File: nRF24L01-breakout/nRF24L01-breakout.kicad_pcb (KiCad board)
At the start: 2 copper layers, 41 x 17.6 mm, 20 parts, among them J1 Conn_01x08_Female, U1 NRF24L01, U2 Antenna_PCB_2.4GHz_50Ohm, Y1 Crystal_GND24_Small

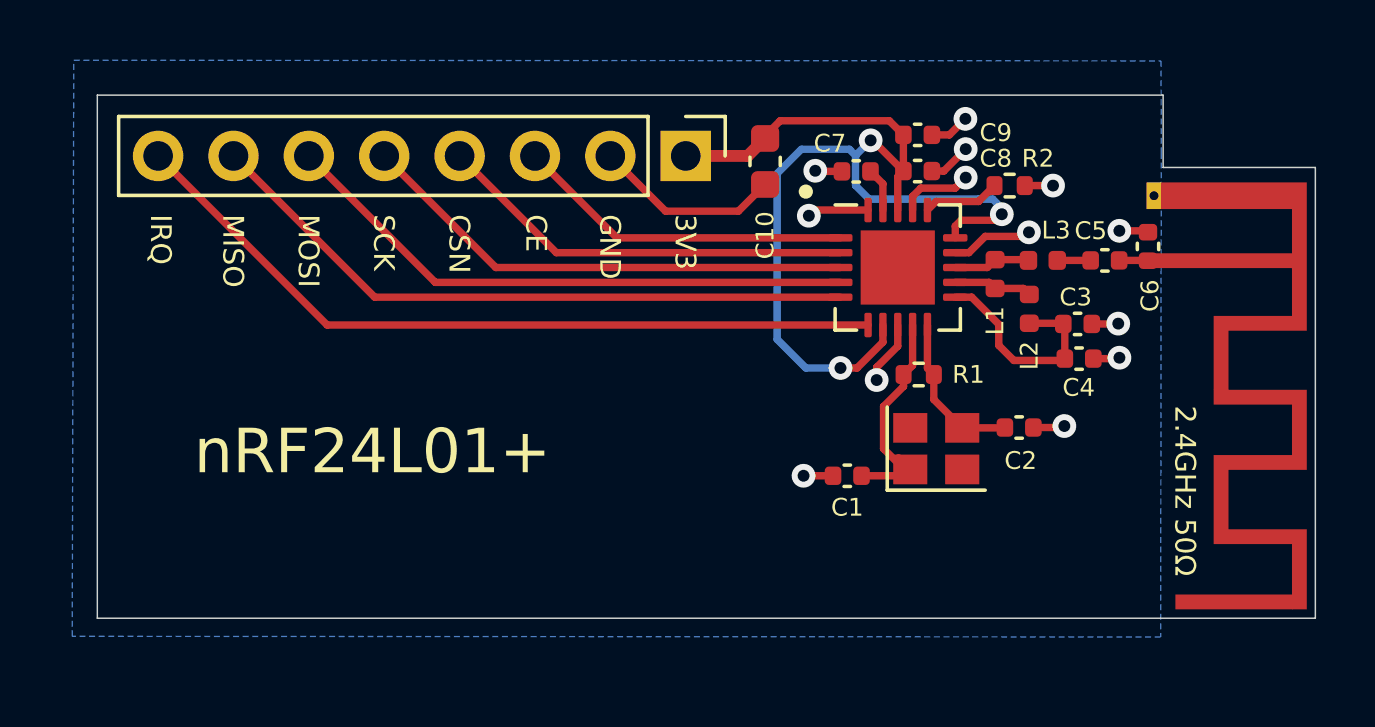
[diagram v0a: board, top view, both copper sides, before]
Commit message: Use Johanson 2450BM14A0002 matched balun
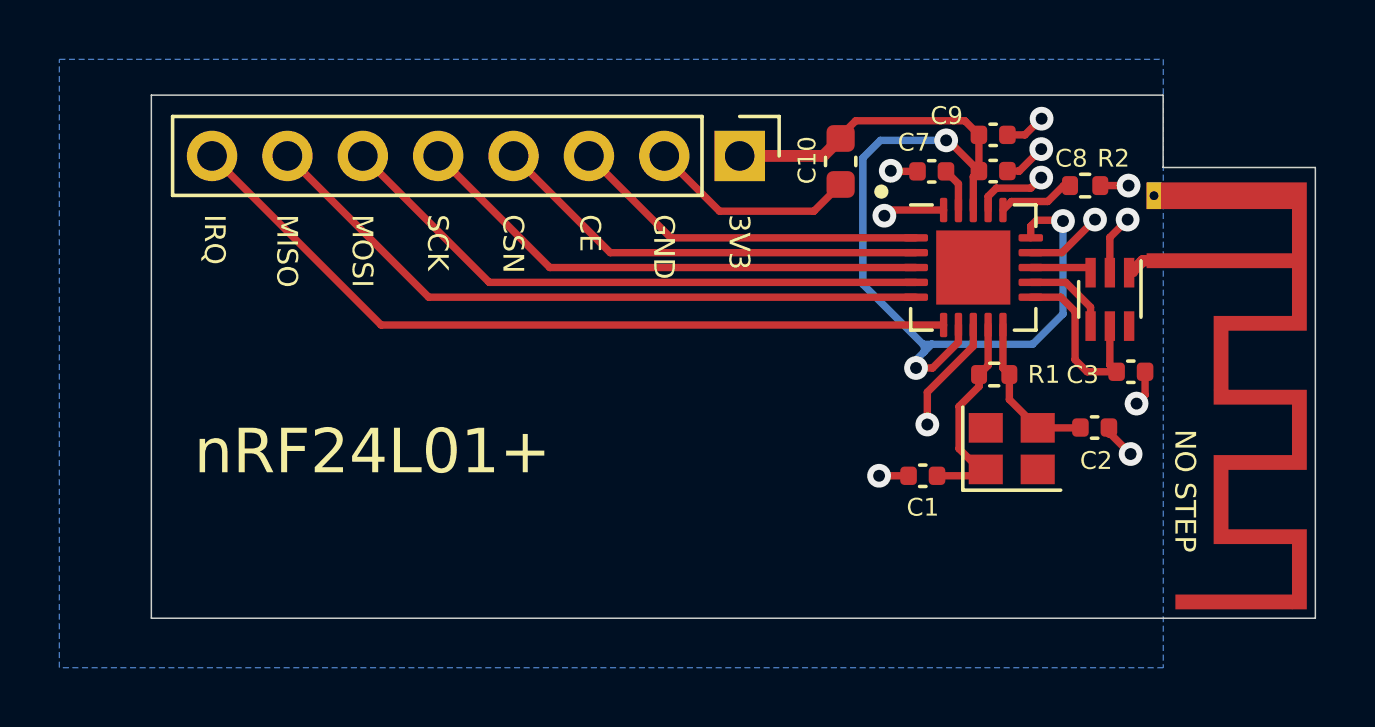
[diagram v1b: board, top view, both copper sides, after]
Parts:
- removed C4: 2.2nF, Capacitor_SMD:C_0402_1005Metric
- removed C5: 1.5pF, Capacitor_SMD:C_0402_1005Metric
- removed C6: 1pF, Capacitor_SMD:C_0402_1005Metric
- removed L1: 8.2nH, Inductor_SMD:L_0402_1005Metric
- removed L2: 2.7nH, Inductor_SMD:L_0402_1005Metric
- removed L3: 3.9nH, Inductor_SMD:L_0402_1005Metric
- added U3: Balun_2450BM14A0002, RF_Converter:Balun_Johanson_0896BM15A0001, F.Cu at (173.6, 90.8)
- moved C1 2.55 mm to (167.3, 96.7)
- moved C2 2.55 mm to (173.1, 95.1)
- moved R1 2.55 mm to (169.7, 93.3)
- moved R2 2.55 mm to (172.7, 86.9)
- moved U1 2.55 mm to (169.0, 89.7)
- moved Y1 2.55 mm to (170.3, 95.8)
- moved C10 2.54 mm to (164.5, 86.1)
- moved C7 2.54 mm to (167.6, 86.4)
- moved C8 2.54 mm to (169.6, 86.4)
- moved C9 2.54 mm to (169.6, 85.2)
- moved C3 2.41 mm to (174.3, 93.2)
- moved J1 1.82 mm to (161.1, 85.9)
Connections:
- net +3V3 renamed VDD
- U2 pad 1: Net-(C5-Pad2) -> Net-(U2-Pad1)
- U2 pad 2: GND -> Net-(U2-Pad1)
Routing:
- net Net-(U2-Pad1): track 0.00 -> 3.31 mm
- net GND: track 25.4 -> 28.6 mm, vias 13 -> 12
- net VDD: track 35.1 -> 36.6 mm
- net Net-(C5-Pad1): track 1.12 -> 0.00 mm
- net Net-(C5-Pad2): track 1.04 -> 0.00 mm
- net VDD_PA: track 7.36 -> 6.52 mm
- net SCK: track 16.9 -> 17.7 mm
- net IRQ: track 26.3 -> 27.0 mm
- net CE: track 11.4 -> 12.2 mm
- net MOSI: track 19.7 -> 20.4 mm
- net MISO: track 22.4 -> 23.1 mm
- net CSN: track 14.2 -> 14.9 mm
- net ANT2: track 2.59 -> 1.99 mm
- net XC2: track 8.05 -> 7.49 mm
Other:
- board size 41 x 17.6 mm -> 39.2 x 17.6 mm
- board text added: "NO STEP"
- board text removed: "2.4GHz 50Ω"
